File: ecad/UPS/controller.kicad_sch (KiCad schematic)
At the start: 32 parts, among them J2 PROG, SW1 SW_Push, SW2 SW_Push, U4 STM32L152RCT6, U5 AP2112K-3.3TRG1

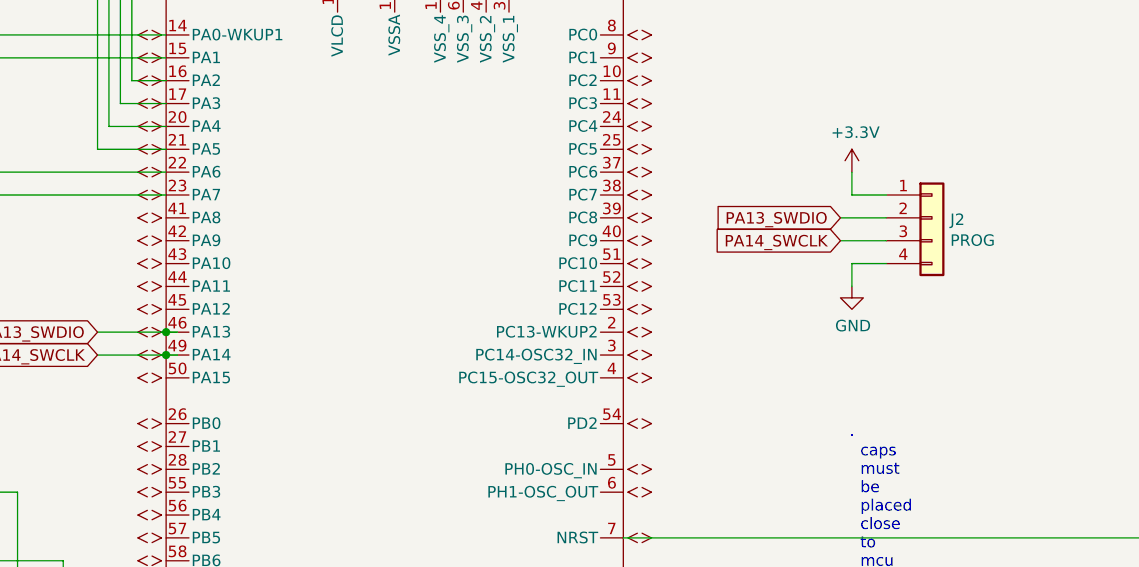
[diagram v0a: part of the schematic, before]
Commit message: Add switch
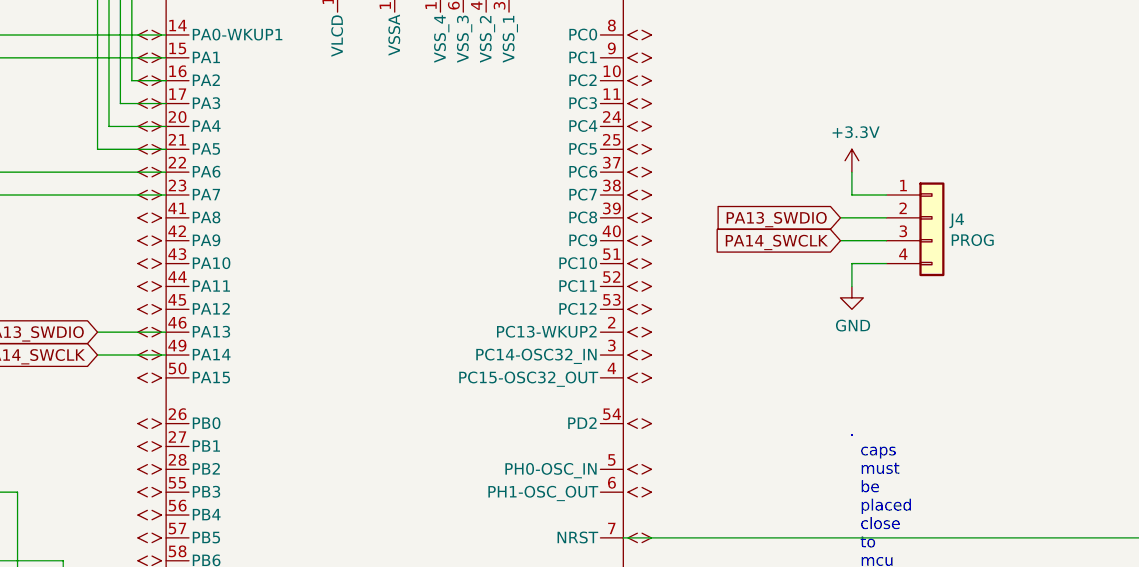
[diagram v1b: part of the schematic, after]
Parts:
- renumbered J2 to J4
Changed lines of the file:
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@@
 	)
 	(junction
-		(at 106.68 81.28)
-		(diameter 0)
-		(color 0 0 0 0)
-	)
-	(junction
 		(at 63.5 139.7)
 		(diameter 0)
@@
 	)
 	(junction
-		(at 106.68 78.74)
-		(diameter 0)
-		(color 0 0 0 0)
-	)
-	(junction
 		(at 228.6 106.68)
 		(diameter 0)
@@
 	(wire
 		(pts
-			(xy 107.95 81.28) (xy 106.68 81.28)
-		)
-		(stroke
-			(width 0)
-			(type default)
-		)
-	)
-	(wire
-		(pts
 			(xy 81.28 20.32) (xy 82.55 20.32)
 		)
@@
 	(wire
 		(pts
+			(xy 99.06 78.74) (xy 106.68 78.74)
+		)
+		(stroke
+			(width 0)
+			(type default)
+		)
+	)
+	(wire
+		(pts
 			(xy 186.69 63.5) (xy 182.88 63.5)
 		)
@@
 	(wire
 		(pts
+			(xy 99.06 81.28) (xy 106.68 81.28)
+		)
+		(stroke
+			(width 0)
+			(type default)
+		)
+	)
+	(wire
+		(pts
 			(xy 106.68 60.96) (xy 62.23 60.96)
 		)
@@
 	(wire
 		(pts
-			(xy 99.06 78.74) (xy 106.68 78.74)
-		)
-		(stroke
-			(width 0)
-			(type default)
-		)
-	)
-	(wire
-		(pts
-			(xy 99.06 81.28) (xy 106.68 81.28)
-		)
-		(stroke
-			(width 0)
-			(type default)
-		)
-	)
-	(wire
-		(pts
 			(xy 31.75 86.36) (xy 62.23 86.36)
 		)
@@
 	(wire
 		(pts
-			(xy 107.95 78.74) (xy 106.68 78.74)
-		)
-		(stroke
-			(width 0)
-			(type default)
-		)
-	)
-	(wire
-		(pts
 			(xy 196.85 115.57) (xy 196.85 113.03)
 		)
@@
 		(on_board yes)
 		(dnp no)
-		(property "Reference" "#PWR?"
+		(property "Reference" "#PWR0120"
 			(at 190.5 115.57 0)
 			(effects
@@
 			(project "UPS"
 				(path "/9d92b60a-4a6b-449c-b462-cab19e69d38c/1d606685-c4fd-4b8c-9a71-b1626d28c437"
-					(reference "#PWR?")
+					(reference "#PWR0120")
 					(unit 1)
 				)
@@
 		(on_board yes)
 		(dnp no)
-		(property "Reference" "#PWR?"
+		(property "Reference" "#PWR0126"
 			(at 182.88 64.77 0)
 			(effects
@@
 			(project "UPS"
 				(path "/9d92b60a-4a6b-449c-b462-cab19e69d38c/1d606685-c4fd-4b8c-9a71-b1626d28c437"
-					(reference "#PWR?")
+					(reference "#PWR0126")
 					(unit 1)
 				)
@@
 		(on_board yes)
 		(dnp no)
-		(property "Reference" "#PWR?"
+		(property "Reference" "#PWR0112"
 			(at 182.88 80.01 0)
 			(effects
@@
 			(project "UPS"
 				(path "/9d92b60a-4a6b-449c-b462-cab19e69d38c/1d606685-c4fd-4b8c-9a71-b1626d28c437"
-					(reference "#PWR?")
+					(reference "#PWR0112")
 					(unit 1)
 				)
@@
 		(on_board yes)
 		(dnp no)
-		(property "Reference" "#PWR?"
+		(property "Reference" "#PWR0110"
 			(at 190.5 142.24 0)
 			(effects
@@
 			(project "UPS"
 				(path "/9d92b60a-4a6b-449c-b462-cab19e69d38c/1d606685-c4fd-4b8c-9a71-b1626d28c437"
-					(reference "#PWR?")
+					(reference "#PWR0110")
 					(unit 1)
 				)
@@
 		(on_board yes)
 		(dnp no)
-		(property "Reference" "J?"
+		(property "Reference" "J4"
 			(at 193.802 66.2432 0)
 			(effects
@@
 			(project "UPS"
 				(path "/9d92b60a-4a6b-449c-b462-cab19e69d38c/1d606685-c4fd-4b8c-9a71-b1626d28c437"
-					(reference "J?")
+					(reference "J4")
 					(unit 1)
 				)

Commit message: Update controller.kicad_sch
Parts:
- added R15, R16: 10k, symbol Device:R
- renumbered C61 to C1, C4 to C2, COUT1 to C3, CIN1 to C4, decouplingcapateachVDDpin5 to C5, decouplingcapateachVDDpin4 to C6, decouplingcapateachVDDpin3 to C7, decouplingcapateachVDDpin2 to C8, decouplingcapateachVDDpin1 to C9, D6 to D1, D10 to D1, D9 to D2, D8 to D4, J4 to J2, R23 to R1, pull-upresistors1 to R10, R33 to R11, R22 to R12, R21 to R13, R20 to R14, R29 to R2, R19 to R3, R18 to R4, otherpullups4 to R5, otherpullups3 to R6, otherpullups2 to R7, otherpullups1 to R8, pull-upresistoronSDA1 to R9, SW2 to SW1, SW1 to SW2, U4 to U1, U5 to U2
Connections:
- net 3.3V: now also R15.2, R16.2
- net vsel1: now reaches U1.43 (PA10)
- net vsel1: now also R15.1
- net vsel2: now reaches U1.44 (PA11)
- net vsel2: now also R16.1
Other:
- moved on the sheet: R5

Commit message: footprints?
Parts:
- C3, C4, C5, C6, C7, C8, C9: footprint (none) -> Capacitor_SMD:C_0805_2012Metric
- R10, R15, R16, R3, R4, R5, R6, R7, R8, R9: footprint (none) -> Resistor_SMD:R_0805_2012Metric
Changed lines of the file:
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@@
 			)
 		)
-		(property "Footprint" ""
+		(property "Footprint" "Resistor_SMD:R_0805_2012Metric"
 			(at 47.498 119.38 90)
 			(effects
@@
 			)
 		)
-		(property "Footprint" ""
+		(property "Footprint" "Capacitor_SMD:C_0805_2012Metric"
 			(at 133.6548 134.62 0)
 			(effects
@@
 			)
 		)
-		(property "Footprint" ""
+		(property "Footprint" "Capacitor_SMD:C_0805_2012Metric"
 			(at 140.0048 134.62 0)
 			(effects
@@
 			)
 		)
-		(property "Footprint" ""
+		(property "Footprint" "Resistor_SMD:R_0805_2012Metric"
 			(at 22.352 100.33 90)
 			(effects
@@
 			)
 		)
-		(property "Footprint" ""
+		(property "Footprint" "Resistor_SMD:R_0805_2012Metric"
 			(at 76.962 119.38 90)
 			(effects
@@
 			)
 		)
-		(property "Footprint" ""
+		(property "Footprint" "Resistor_SMD:R_0805_2012Metric"
 			(at 80.772 119.38 90)
 			(effects
@@
 			)
 		)
-		(property "Footprint" ""
+		(property "Footprint" "Resistor_SMD:R_0805_2012Metric"
 			(at 66.802 119.38 90)
 			(effects
@@
 			)
 		)
-		(property "Footprint" ""
+		(property "Footprint" "Resistor_SMD:R_0805_2012Metric"
 			(at 51.308 119.38 90)
 			(effects
@@
 			)
 		)
-		(property "Footprint" ""
+		(property "Footprint" "Capacitor_SMD:C_0805_2012Metric"
 			(at 123.4948 134.62 0)
 			(effects
@@
 			)
 		)
-		(property "Footprint" ""
+		(property "Footprint" "Capacitor_SMD:C_0805_2012Metric"
 			(at 93.0148 156.21 0)
 			(effects
@@
 			)
 		)
-		(property "Footprint" ""
+		(property "Footprint" "Resistor_SMD:R_0805_2012Metric"
 			(at 88.392 118.11 90)
 			(effects
@@
 			)
 		)
-		(property "Footprint" ""
+		(property "Footprint" "Resistor_SMD:R_0805_2012Metric"
 			(at 56.642 119.38 90)
 			(effects
@@
 			)
 		)
-		(property "Footprint" ""
+		(property "Footprint" "Capacitor_SMD:C_0805_2012Metric"
 			(at 47.2948 153.67 0)
 			(effects
@@
 			)
 		)
-		(property "Footprint" ""
+		(property "Footprint" "Capacitor_SMD:C_0805_2012Metric"
 			(at 118.4148 134.62 0)
 			(effects
@@
 			)
 		)
-		(property "Footprint" ""
+		(property "Footprint" "Resistor_SMD:R_0805_2012Metric"
 			(at 71.882 119.38 90)
 			(effects
@@
 			)
 		)
-		(property "Footprint" ""
+		(property "Footprint" "Resistor_SMD:R_0805_2012Metric"
 			(at 61.722 119.38 90)
 			(effects
@@
 			)
 		)
-		(property "Footprint" ""
+		(property "Footprint" "Capacitor_SMD:C_0805_2012Metric"
 			(at 128.5748 134.62 0)
 			(effects

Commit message: Output section of PCB
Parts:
- renumbered C2 to C4, C1 to C61, C4 to CIN1, C3 to COUT1, D1 to D10, D1 to D6, D4 to D8, D2 to D9, J2 to J4, R4 to R18, R3 to R19, R14 to R20, R13 to R21, R12 to R22, R1 to R23, R2 to R29, R11 to R33, R15 to R36, R16 to R37, SW2 to SW1, SW1 to SW2, U1 to U4, U2 to U5, C9 to decouplingcapateachVDDpin1, C8 to decouplingcapateachVDDpin2, C7 to decouplingcapateachVDDpin3, C6 to decouplingcapateachVDDpin4, C5 to decouplingcapateachVDDpin5, R8 to otherpullups1, R7 to otherpullups2, R6 to otherpullups3, R5 to otherpullups4, R9 to pull-upresistoronSDA1, R10 to pull-upresistors1
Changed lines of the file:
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@@
 		(on_board yes)
 		(dnp no)
-		(property "Reference" "#PWR012"
+		(property "Reference" "#PWR0118"
 			(at 48.26 161.29 0)
 			(effects
@@
 		(on_board yes)
 		(dnp no)
-		(property "Reference" "#PWR013"
+		(property "Reference" "#PWR0119"
 			(at 48.26 147.32 0)
 			(effects
@@
 		(on_board yes)
 		(dnp no)
-		(property "Reference" "#PWR04"
+		(property "Reference" "#PWR0113"
 			(at 228.6 125.73 0)
 			(effects
@@
 		(on_board yes)
 		(dnp no)
-		(property "Reference" "SW1"
+		(property "Reference" "SW2"
 			(at 242.189 114.3 0)
 			(effects
@@
 		(on_board yes)
 		(dnp no)
-		(property "Reference" "#PWR05"
+		(property "Reference" "#PWR0114"
 			(at 228.6 99.06 0)
 			(effects
@@
 		(on_board yes)
 		(dnp no)
-		(property "Reference" "#PWR024"
+		(property "Reference" "#PWR0124"
 			(at 74.93 34.29 0)
 			(effects
@@
 		(on_board yes)
 		(dnp no)
-		(property "Reference" "R10"
+		(property "Reference" "pull-upresistors1"
 			(at 38.354 117.856 0)
 			(effects
@@
 		(on_board yes)
 		(dnp no)
-		(property "Reference" "D1"
+		(property "Reference" "D6"
 			(at 93.7006 37.2872 90)
 			(effects
@@
 		(dnp no)
 		(fields_autoplaced yes)
-		(property "Reference" "C6"
+		(property "Reference" "decouplingcapateachVDDpin4"
 			(at 138.43 137.1599 0)
 			(effects
@@
 		(on_board yes)
 		(dnp no)
-		(property "Reference" "C1"
+		(property "Reference" "C61"
 			(at 188.1632 121.8184 0)
 			(effects
@@
 		(on_board yes)
 		(dnp no)
-		(property "Reference" "R2"
+		(property "Reference" "R29"
 			(at 227.1014 128.1684 0)
 			(effects
@@
 		(on_board yes)
 		(dnp no)
-		(property "Reference" "R13"
+		(property "Reference" "R21"
 			(at 86.2584 21.8186 0)
 			(effects
@@
 		(on_board yes)
 		(dnp no)
-		(property "Reference" "D2"
+		(property "Reference" "D9"
 			(at 93.7006 23.3172 90)
 			(effects
@@
 		(dnp no)
 		(fields_autoplaced yes)
-		(property "Reference" "C5"
+		(property "Reference" "decouplingcapateachVDDpin5"
 			(at 144.78 137.1599 0)
 			(effects
@@
 		(on_board yes)
 		(dnp no)
-		(property "Reference" "R11"
+		(property "Reference" "R33"
 			(at 86.2584 35.7886 0)
 			(effects
@@
 		(on_board yes)
 		(dnp no)
-		(property "Reference" "R12"
+		(property "Reference" "R22"
 			(at 86.2584 29.4386 0)
 			(effects
@@
 		(on_board yes)
 		(dnp no)
-		(property "Reference" "#PWR014"
+		(property "Reference" "#PWR0120"
 			(at 190.5 115.57 0)
 			(effects
@@
 		(on_board yes)
 		(dnp no)
-		(property "Reference" "#PWR09"
+		(property "Reference" "#PWR0121"
 			(at 74.93 16.51 0)
 			(effects
@@
 		(dnp no)
 		(fields_autoplaced yes)
-		(property "Reference" "R4"
+		(property "Reference" "R18"
 			(at 26.67 99.0599 0)
 			(effects
@@
 		(on_board yes)
 		(dnp no)
-		(property "Reference" "#PWR07"
+		(property "Reference" "#PWR0123"
 			(at 74.93 27.94 0)
 			(effects
@@
 		(on_board yes)
 		(dnp no)
-		(property "Reference" "#PWR06"
+		(property "Reference" "#PWR0111"
 			(at 140.97 153.67 0)
 			(effects
@@
 		(dnp no)
 		(fields_autoplaced yes)
-		(property "Reference" "U2"
+		(property "Reference" "U5"
 			(at 73.66 153.67 0)
 			(effects
@@
 		(on_board yes)
 		(dnp no)
-		(property "Reference" "#PWR010"
+		(property "Reference" "#PWR0125"
 			(at 116.84 38.1 0)
 			(effects
@@
 		(on_board yes)
 		(dnp no)
-		(property "Reference" "SW2"
+		(property "Reference" "SW1"
 			(at 204.089 120.65 0)
 			(effects
@@
 		(on_board yes)
 		(dnp no)
-		(property "Reference" "#PWR02"
+		(property "Reference" "#PWR0116"
 			(at 53.34 172.72 0)
 			(effects
@@
 		(dnp no)
 		(fields_autoplaced yes)
-		(property "Reference" "R16"
+		(property "Reference" "R37"
 			(at 81.28 118.1099 0)
 			(effects
@@
 				)
 			)
+			(project "UPS"
+				(path "/9d92b60a-4a6b-449c-b462-cab19e69d38c/1d606685-c4fd-4b8c-9a71-b1626d28c437"
+					(reference "R37")
+					(unit 1)
+				)
+			)
 		)
 	)
@@
 		(on_board yes)
 		(dnp no)
-		(property "Reference" "D4"
+		(property "Reference" "D8"
 			(at 93.7006 20.7772 90)
 			(effects
@@
 		(on_board yes)
 		(dnp no)
-		(property "Reference" "#PWR015"
+		(property "Reference" "#PWR0126"
 			(at 182.88 64.77 0)
 			(effects
@@
 		(on_board yes)
 		(dnp no)
-		(property "Reference" "D1"
+		(property "Reference" "D10"
 			(at 93.7006 30.9372 90)
 			(effects
@@
 		(dnp no)
 		(fields_autoplaced yes)
-		(property "Reference" "R5"
+		(property "Reference" "otherpullups4"
 			(at 85.09 118.1099 0)
 			(effects
@@
 		(dnp no)
 		(fields_autoplaced yes)
-		(property "Reference" "R6"
+		(property "Reference" "otherpullups3"
 			(at 71.12 118.1099 0)
 			(effects
@@
 		(dnp no)
 		(fields_autoplaced yes)
-		(property "Reference" "R9"
+		(property "Reference" "pull-upresistoronSDA1"
 			(at 52.07 118.1099 0)
 			(effects
@@
 		(dnp no)
 		(fields_autoplaced yes)
-		(property "Reference" "C8"
+		(property "Reference" "decouplingcapateachVDDpin2"
 			(at 128.27 137.1599 0)
 			(effects
@@
 		(on_board yes)
 		(dnp no)
-		(property "Reference" "#PWR016"
+		(property "Reference" "#PWR0112"
 			(at 182.88 80.01 0)
 			(effects
@@
 		(on_board yes)
 		(dnp no)
-		(property "Reference" "R1"
+		(property "Reference" "R23"
 			(at 189.0014 134.5184 0)
 			(effects
@@
 		(on_board yes)
 		(dnp no)
-		(property "Reference" "#PWR011"
+		(property "Reference" "#PWR0110"
 			(at 190.5 142.24 0)
 			(effects
@@
 		(dnp no)
 		(fields_autoplaced yes)
-		(property "Reference" "C3"
+		(property "Reference" "COUT1"
 			(at 97.79 158.7499 0)
 			(effects
@@
 		(dnp no)
 		(fields_autoplaced yes)
-		(property "Reference" "R3"
+		(property "Reference" "R19"
 			(at 92.71 116.8399 0)
 			(effects
@@
 		(dnp no)
 		(fields_autoplaced yes)
-		(property "Reference" "R8"
+		(property "Reference" "otherpullups1"
 			(at 60.96 118.1099 0)
 			(effects
@@
 		(on_board yes)
 		(dnp no)
-		(property "Reference" "J2"
+		(property "Reference" "J4"
 			(at 193.802 66.2432 0)
 			(effects
@@
 		(on_board yes)
 		(dnp no)
-		(property "Reference" "C2"
+		(property "Reference" "C4"
 			(at 226.2632 115.4684 0)
 			(effects
@@
 		(on_board yes)
 		(dnp no)
-		(property "Reference" "#PWR?"
+		(property "Reference" "#PWR051"
 			(at 114.3 162.56 0)
 			(effects
@@
 		(dnp no)
 		(fields_autoplaced yes)
-		(property "Reference" "C4"
+		(property "Reference" "CIN1"
 			(at 52.07 156.2099 0)
 			(effects
@@
 		(on_board yes)
 		(dnp no)
-		(property "Reference" "R14"
+		(property "Reference" "R20"
 			(at 86.2584 19.2786 0)
 			(effects
@@
 		(dnp no)
 		(fields_autoplaced yes)
-		(property "Reference" "C9"
+		(property "Reference" "decouplingcapateachVDDpin1"
 			(at 123.19 137.1599 0)
 			(effects
@@
 		(on_board yes)
 		(dnp no)
-		(property "Reference" "#PWR01"
+		(property "Reference" "#PWR0115"
 			(at 93.98 149.86 0)
 			(effects
@@
 		(dnp no)
 		(fields_autoplaced yes)
-		(property "Reference" "R15"
+		(property "Reference" "R36"
 			(at 76.2 118.1099 0)
 			(effects
@@
 				)
 			)
+			(project "UPS"
+				(path "/9d92b60a-4a6b-449c-b462-cab19e69d38c/1d606685-c4fd-4b8c-9a71-b1626d28c437"
+					(reference "R36")
+					(unit 1)
+				)
+			)
 		)
 	)
@@
 		(dnp no)
 		(fields_autoplaced yes)
-		(property "Reference" "R7"
+		(property "Reference" "otherpullups2"
 			(at 66.04 118.1099 0)
 			(effects
@@
 		(dnp no)
 		(fields_autoplaced yes)
-		(property "Reference" "C7"
+		(property "Reference" "decouplingcapateachVDDpin3"
 			(at 133.35 137.1599 0)
 			(effects
@@
 		(on_board yes)
 		(dnp no)
-		(property "Reference" "U1"
+		(property "Reference" "U4"
 			(at 129.54 116.586 0)
 			(effects
@@
 		(dnp no)
 		(fields_autoplaced yes)
-		(property "Reference" "#PWR03"
+		(property "Reference" "#PWR0109"
 			(at 24.13 110.49 0)
 			(effects
@@
 		(on_board yes)
 		(dnp no)
-		(property "Reference" "#PWR08"
+		(property "Reference" "#PWR0122"
 			(at 74.93 20.32 0)
 			(effects

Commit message: push button foot print
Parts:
- removed SW1, SW2: SW_Push, Button_Switch_SMD:SW_SPST_B3U-1000P-B, symbol Switch:SW_Push
- added U6, U7: B3U-1000P-B, B3U-1000P-B, symbol UPS:B3U-1000P-B
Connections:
- net 3.3V: now also U6.2
- net GND: now also U7.2
- net NRST: now also U7.1
- net at C61.1, R23.2, U4.60 (BOOT0): now also U6.1

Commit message: Ty's VBATSENSE Changes
Let me know if I messed this part up, did a small amount
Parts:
- added C65: 1nF, Capacitor_SMD:C_0603_1608Metric_Pad1.08x0.95mm_HandSolder, symbol Device:C
- added R42: 4.7k, Resistor_SMD:R_0805_2012Metric, symbol Device:R
- U6: value B3U-1000P-B -> BOOT0
- U7: value B3U-1000P-B -> NRST
- renumbered decouplingcapateachVDDpin1 to C27, decouplingcapateachVDDpin2 to C49, decouplingcapateachVDDpin3 to C50, decouplingcapateachVDDpin4 to C62, decouplingcapateachVDDpin5 to C63, pull-upresistoronSDA1 to R10, otherpullups1 to R12, otherpullups2 to R15, otherpullups3 to R16, otherpullups4 to R39, pull-upresistors1 to R9
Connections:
- net +3.3V: now also C27.2, C49.2, C50.2, C62.2, C63.2, COUT1.1, R10.1, R12.2, R15.2, R16.2, R19.2, R36.2, R37.2, R39.2, R9.1, U4.13 (VDDA), U4.19 (VDD_4), U4.32 (VDD_1), U4.48 (VDD_2), U4.64 (VDD_3), U5.5 (VOUT)
- net 3.3V: no longer C27.2, C49.2, C50.2, C62.2, C63.2, COUT1.1, R10.1, R12.2, R15.2, R16.2, R19.2, R36.2, R37.2, R39.2, R9.1, U4.13 (VDDA), U4.19 (VDD_4), U4.32 (VDD_1), U4.48 (VDD_2), U4.64 (VDD_3), U5.5 (VOUT)
- net at D6.2 (A): now also U4.42 (PA9); no longer U4.21 (PA5)
- net at D10.2 (A): now also U4.41 (PA8); no longer U4.20 (PA4)
- new net: C65.2, R42.2
- new net: R42.1, U4.20 (PA4)
- new net vbat_sense: C65.1
